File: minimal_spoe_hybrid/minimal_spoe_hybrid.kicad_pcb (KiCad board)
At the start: 4 copper layers, 25.4 x 20.3 mm, 4 parts, among them J1 TBP02R2-381-03BE

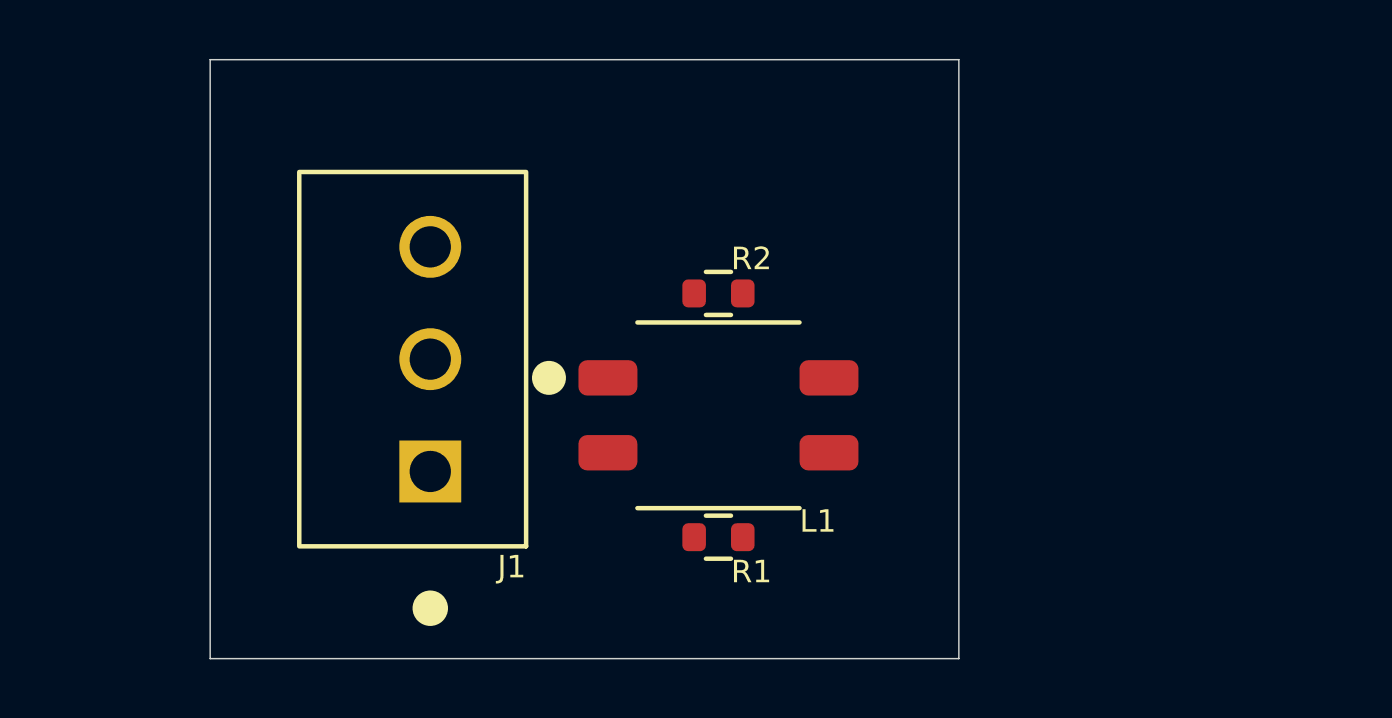
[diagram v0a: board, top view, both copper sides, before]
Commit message: Update KiCAD Symbol Generator submodule and modify project settings
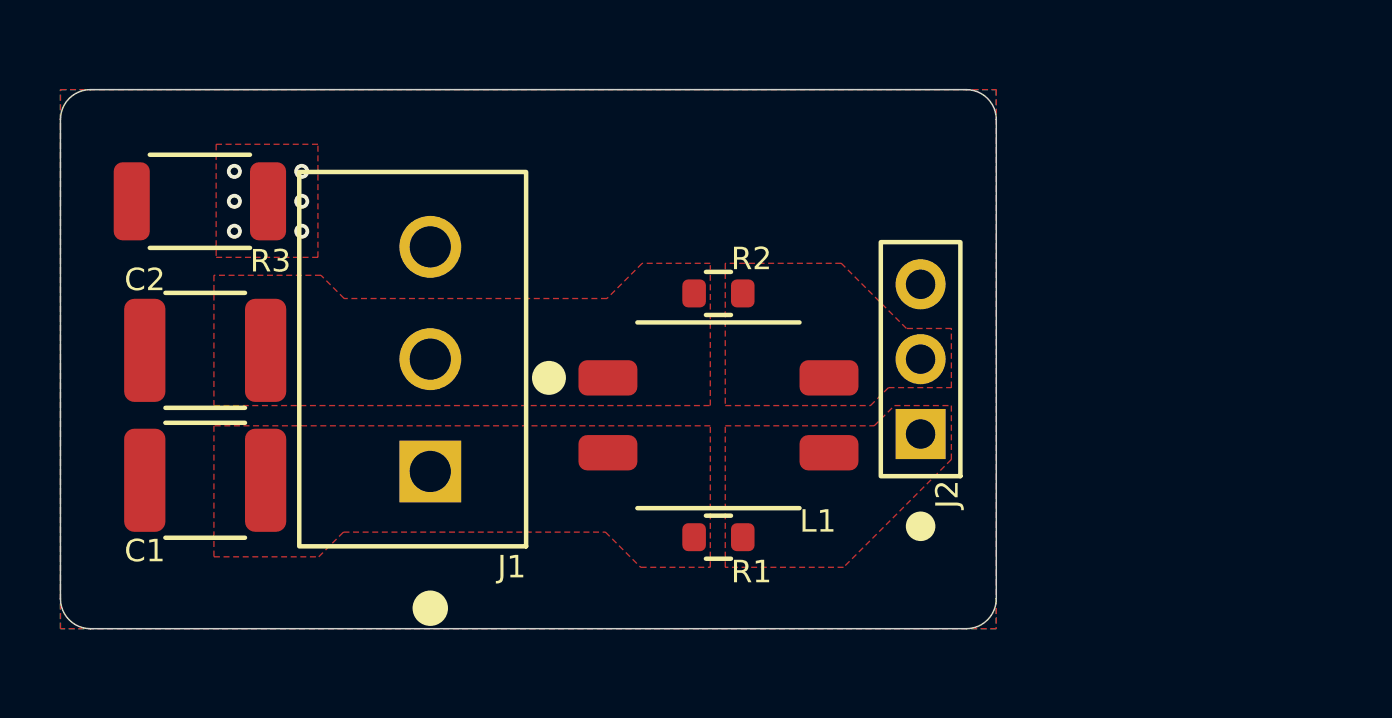
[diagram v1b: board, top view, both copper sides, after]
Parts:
- added C1: 100 pF, capacitor_footprints:C_1812_4532Metric, F.Cu at (121.5, 112.8)
- added C2: 100 pF, capacitor_footprints:C_1812_4532Metric, F.Cu at (121.5, 108.4)
- added J2: TSW-103-14-G-S, connector_footprints:TSW-103-14-G-S, F.Cu at (145.8, 108.7)
- added R3: 4.7 MΩ, resistor_footprints:R_2010_5025Metric, F.Cu at (121.3, 103.3)
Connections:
- net Net-(J1-Pad1) renamed /CABLE+
- net Net-(J1-Pad2) renamed /CABLE-
- net Net-(L1-Pad3) renamed /DATA_AND_POWER_P
- net Net-(L1-Pad4) renamed /DATA_AND_POWER_N
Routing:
- net GND: vias 0 -> 6
- added copper zone on F.Cu, net /CABLE+
- added copper zone on F.Cu, net /CABLE-
- added copper zone on F.Cu, net /DATA_AND_POWER_N
- added copper zone on F.Cu, net /DATA_AND_POWER_P
- added copper zone on F.Cu, net Earth
- added copper zone on In1.Cu, net Earth
- added copper zone on In2.Cu, net Earth
- added copper zone on B.Cu, net GND
- added copper zone on F.Cu, net GND
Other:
- board size 25.4 x 20.3 mm -> 31.8 x 18.3 mm

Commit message: Update KiCAD Symbol Generator submodule and modify project configuration
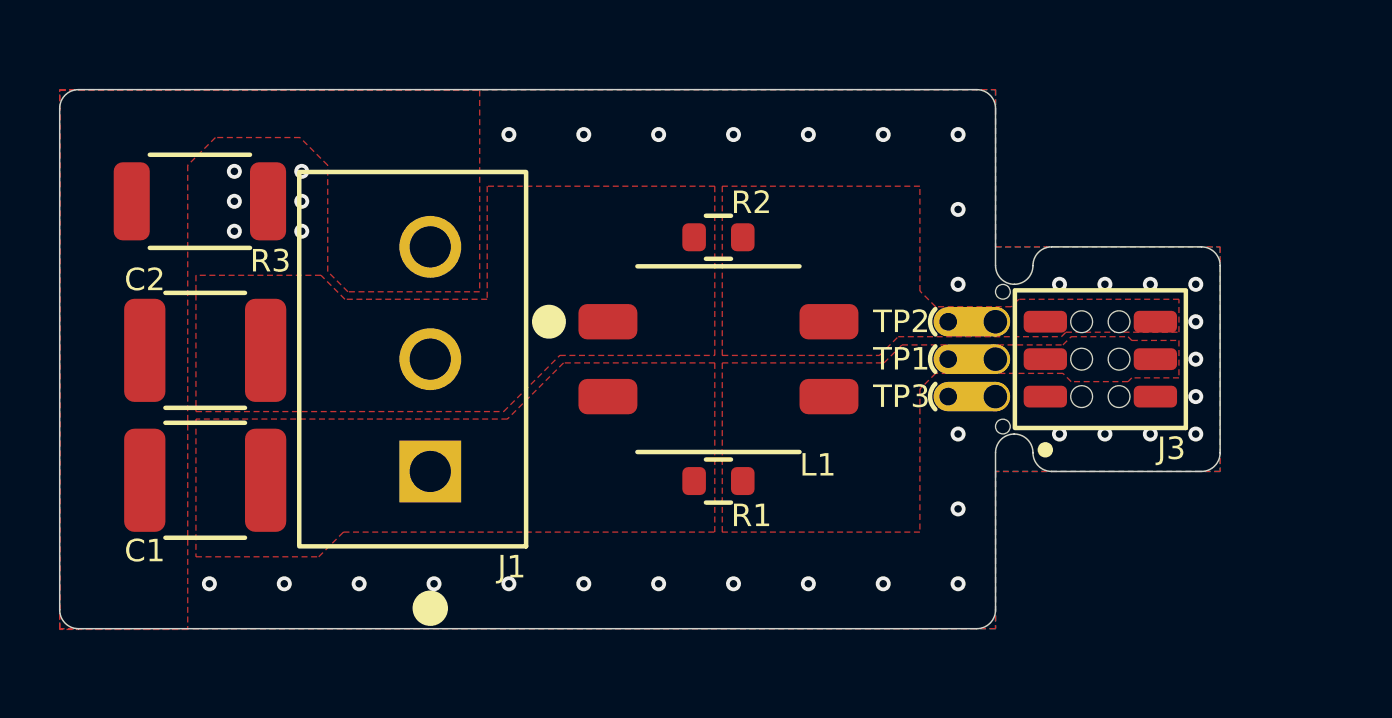
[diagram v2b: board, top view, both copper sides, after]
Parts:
- removed J2: TSW-103-14-G-S, connector_footprints:TSW-103-14-G-S
- added J3: CLP-103-02-G-D-BE, connector_footprints:CLP-103-02-G-D-BE, F.Cu at (151.9, 108.7)
- added MB1: mouse-bite-midle-50mil-200mil, mouse_bite_footprints:mouse-bite-midle-50mil-250mil, F.Cu at (149.0, 108.7)
- added TP1: TestPoint, test_point_footprints:TestPoint_THTPad_Castelated, F.Cu at (148.3, 108.7)
- added TP2: TestPoint, test_point_footprints:TestPoint_THTPad_Castelated, F.Cu at (148.3, 107.4)
- added TP3: TestPoint, test_point_footprints:TestPoint_THTPad_Castelated, F.Cu at (148.3, 110.0)
- moved L1 1.91 mm to (138.9, 108.7)
- moved R1 1.91 mm to (138.9, 112.8)
- moved R2 1.91 mm to (138.9, 104.6)
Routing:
- net GND: vias 6 -> 39
- added copper zone on In1.Cu, net GND
- added copper zone on In2.Cu, net GND
- removed copper zone on In2.Cu, net Earth
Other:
- board size 31.8 x 18.3 mm -> 39.4 x 18.3 mm

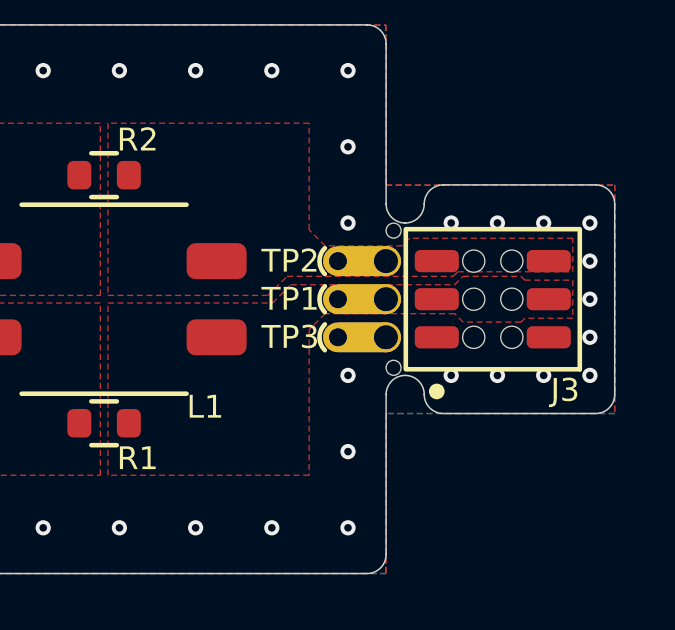
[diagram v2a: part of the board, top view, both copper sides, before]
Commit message: Update KiCAD Symbol Generator submodule and remove unused circle elements from schematic
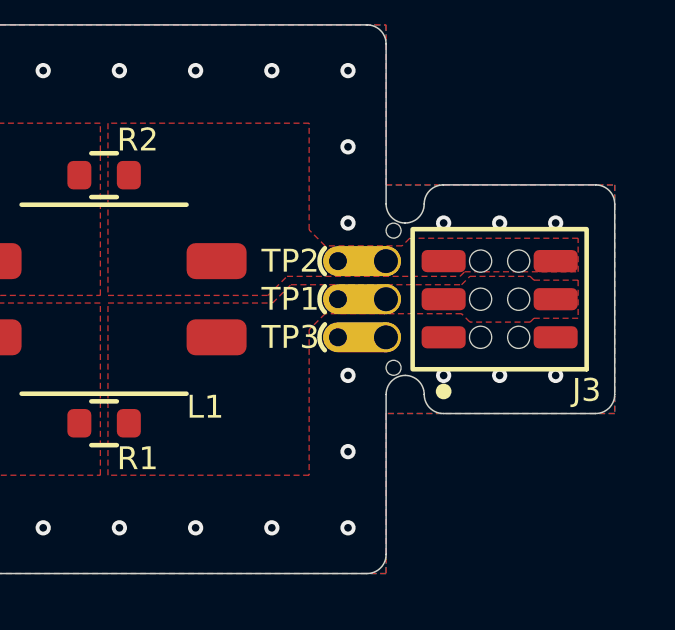
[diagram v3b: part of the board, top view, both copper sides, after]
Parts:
- moved J3 0.23 mm to (152.1, 108.7)
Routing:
- net GND: vias 39 -> 34
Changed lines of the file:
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@@
 	(footprint "connector_footprints:CLP-103-02-G-D-BE"
 		(layer "F.Cu")
-		(at 151.8921 108.6866 90)
+		(at 152.1207 108.6866 90)
 		(property "Reference" "J3"
 			(at -2.589 2.9 0)
@@
 					(thickness 0.1524)
 				)
-				(justify right top)
+				(justify top)
 			)
 		)
@@
 	)
 	(via
-		(at 155.129099 109.9566)
-		(size 0.508)
-		(drill 0.254)
-		(layers "F.Cu" "B.Cu")
-		(free yes)
-		(net 4)
-	)
-	(via
 		(at 129.286 116.3066)
 		(size 0.508)
@@
 	)
 	(via
-		(at 150.506099 106.1466)
-		(size 0.508)
-		(drill 0.254)
-		(layers "F.Cu" "B.Cu")
-		(free yes)
-		(net 4)
-	)
-	(via
-		(at 150.506099 111.2266)
+		(at 150.2537 106.1466)
+		(size 0.508)
+		(drill 0.254)
+		(layers "F.Cu" "B.Cu")
+		(free yes)
+		(net 4)
+	)
+	(via
+		(at 150.2537 111.2266)
 		(size 0.508)
 		(drill 0.254)
@@
 	)
 	(via
-		(at 152.047099 106.1466)
+		(at 152.1207 106.1466)
 		(size 0.508)
 		(drill 0.254)
@@
 	)
 	(via
-		(at 155.129099 108.6866)
-		(size 0.508)
-		(drill 0.254)
-		(layers "F.Cu" "B.Cu")
-		(free yes)
-		(net 4)
-	)
-	(via
-		(at 155.129099 106.1466)
-		(size 0.508)
-		(drill 0.254)
-		(layers "F.Cu" "B.Cu")
-		(free yes)
-		(net 4)
-	)
-	(via
 		(at 147.066 116.3066)
 		(size 0.508)
@@
 	)
 	(via
-		(at 152.047099 111.2266)
+		(at 152.1207 111.2266)
 		(size 0.508)
 		(drill 0.254)
@@
 	)
 	(via
-		(at 155.129099 111.2266)
-		(size 0.508)
-		(drill 0.254)
-		(layers "F.Cu" "B.Cu")
-		(free yes)
-		(net 4)
-	)
-	(via
 		(at 124.206 116.3066)
 		(size 0.508)
@@
 	)
 	(via
-		(at 153.588099 106.1466)
+		(at 153.9877 106.1466)
 		(size 0.508)
 		(drill 0.254)
@@
 	)
 	(via
-		(at 155.129099 107.4166)
-		(size 0.508)
-		(drill 0.254)
-		(layers "F.Cu" "B.Cu")
-		(free yes)
-		(net 4)
-	)
-	(via
-		(at 153.588099 111.2266)
+		(at 153.9877 111.2266)
 		(size 0.508)
 		(drill 0.254)
@@
 		(polygon
 			(pts
-				(xy 139.065 114.554) (xy 139.065 108.8136) (xy 144.5514 108.8136) (xy 145.161 108.204) (xy 150.622 108.204)
-				(xy 150.9014 107.9246) (xy 152.8318 107.9246) (xy 152.9588 108.0516) (xy 154.559 108.0516) (xy 154.559 109.3216)
-				(xy 152.9588 109.3216) (xy 152.8318 109.4486) (xy 150.9014 109.4486) (xy 150.622 109.1692) (xy 146.304 109.1692)
+				(xy 139.065 114.554) (xy 139.065 108.8136) (xy 144.5514 108.8136) (xy 145.161 108.204) (xy 150.8506 108.204)
+				(xy 151.13 107.9246) (xy 153.1366 107.9246) (xy 153.2636 108.0516) (xy 154.7368 108.0516) (xy 154.7368 109.3216)
+				(xy 153.2636 109.3216) (xy 153.1366 109.4486) (xy 151.13 109.4486) (xy 150.8506 109.1692) (xy 146.304 109.1692)
 				(xy 145.7706 109.7026) (xy 145.7706 114.554)
 			)
@@
 			(pts
 				(xy 145.7706 102.8192) (xy 139.065 102.8192) (xy 139.065 108.5596) (xy 144.399 108.5596) (xy 145.034 107.9246)
-				(xy 150.5712 107.9246) (xy 150.7236 107.7722) (xy 154.559 107.7722) (xy 154.559 106.6546) (xy 149.1234 106.6546)
+				(xy 150.7998 107.9246) (xy 150.9522 107.7722) (xy 154.7368 107.7722) (xy 154.7368 106.6546) (xy 149.1234 106.6546)
 				(xy 148.8694 106.9086) (xy 146.304 106.9086) (xy 145.7706 106.3752)
 			)

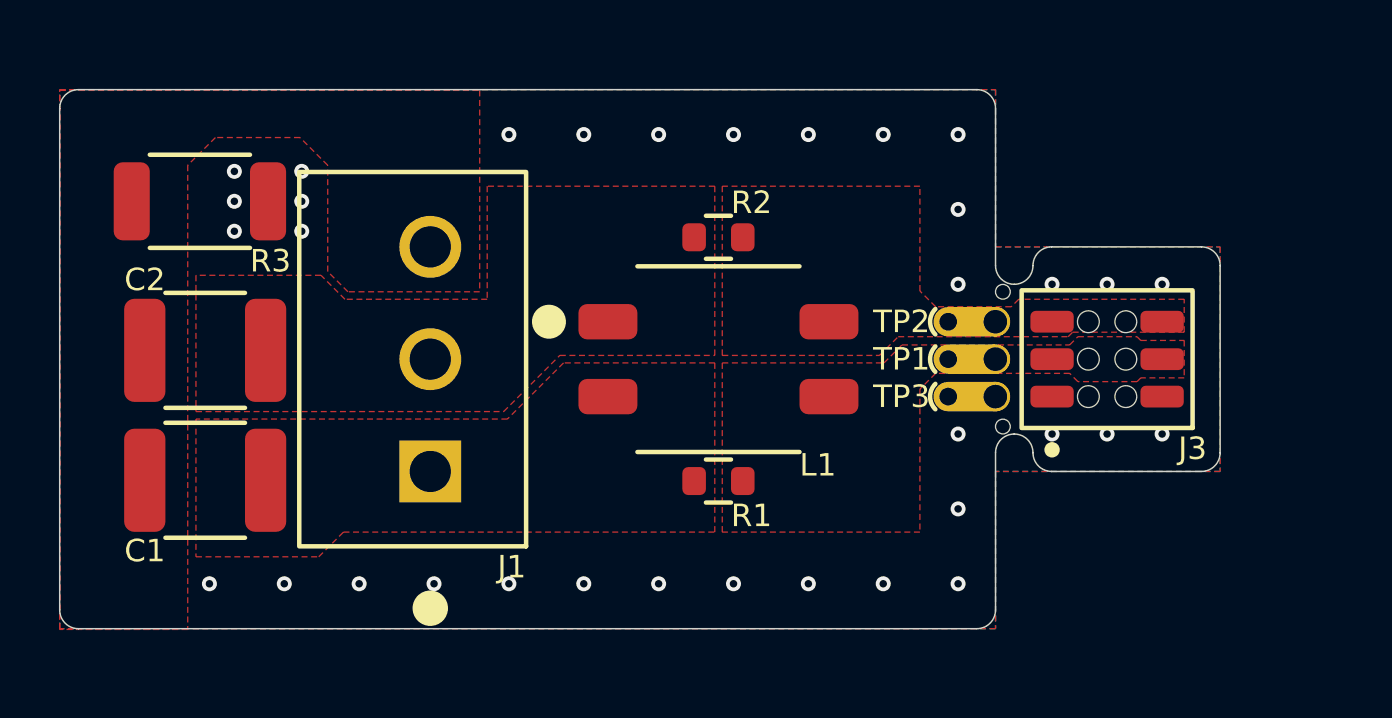
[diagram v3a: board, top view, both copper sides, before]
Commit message: Update KiCAD Symbol Generator submodule and clean up project configuration
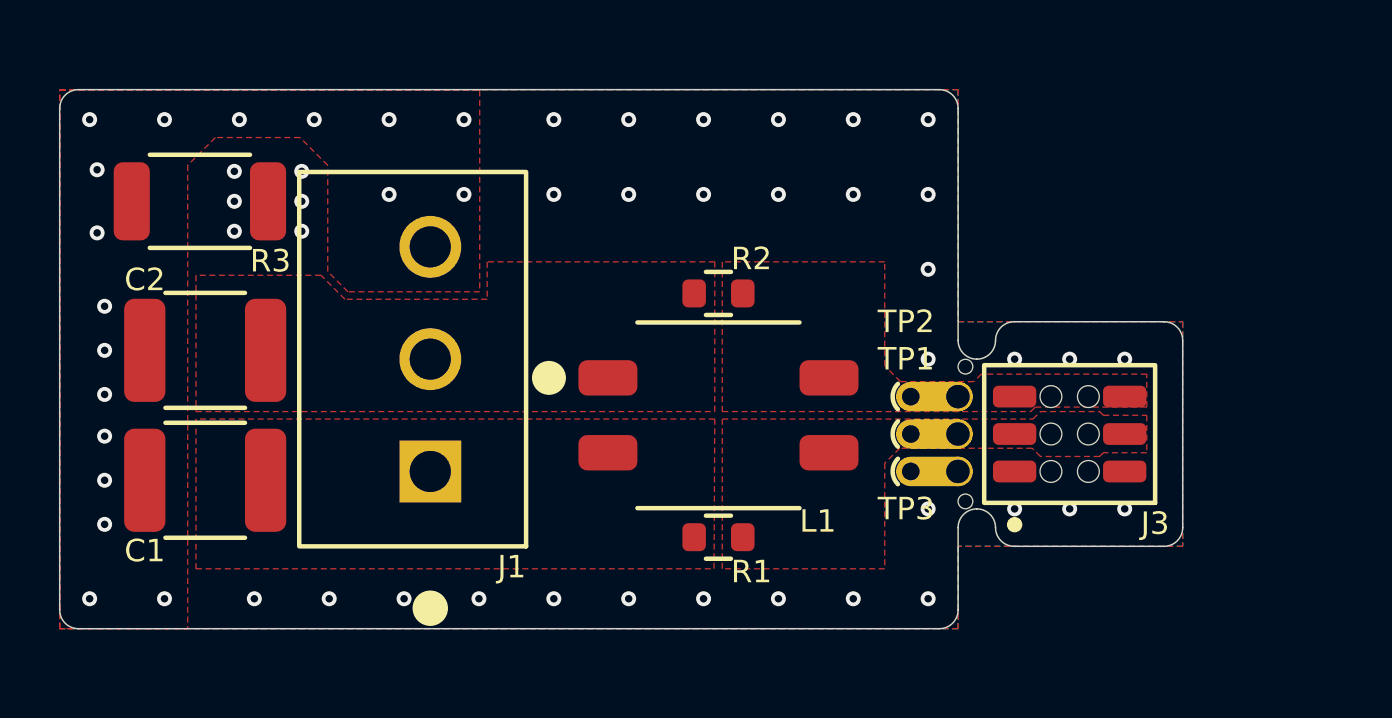
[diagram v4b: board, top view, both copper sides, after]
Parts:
- moved J3 2.84 mm to (150.9, 111.2)
- moved MB1 2.84 mm to (147.7, 111.2)
- moved TP1 2.84 mm to (147.1, 111.2)
- moved TP3 2.84 mm to (147.1, 112.5)
- moved TP2 2.84 mm to (147.1, 110.0)
- moved L1 1.91 mm to (138.9, 110.6)
- moved R1 1.91 mm to (138.9, 114.7)
- moved R2 1.91 mm to (138.9, 106.5)
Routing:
- net GND: vias 34 -> 37
- net Earth: vias 0 -> 18
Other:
- board size 39.4 x 18.3 mm -> 38.1 x 18.3 mm

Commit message: Update KiCAD Symbol Generator submodule and regenerate PDF schematic
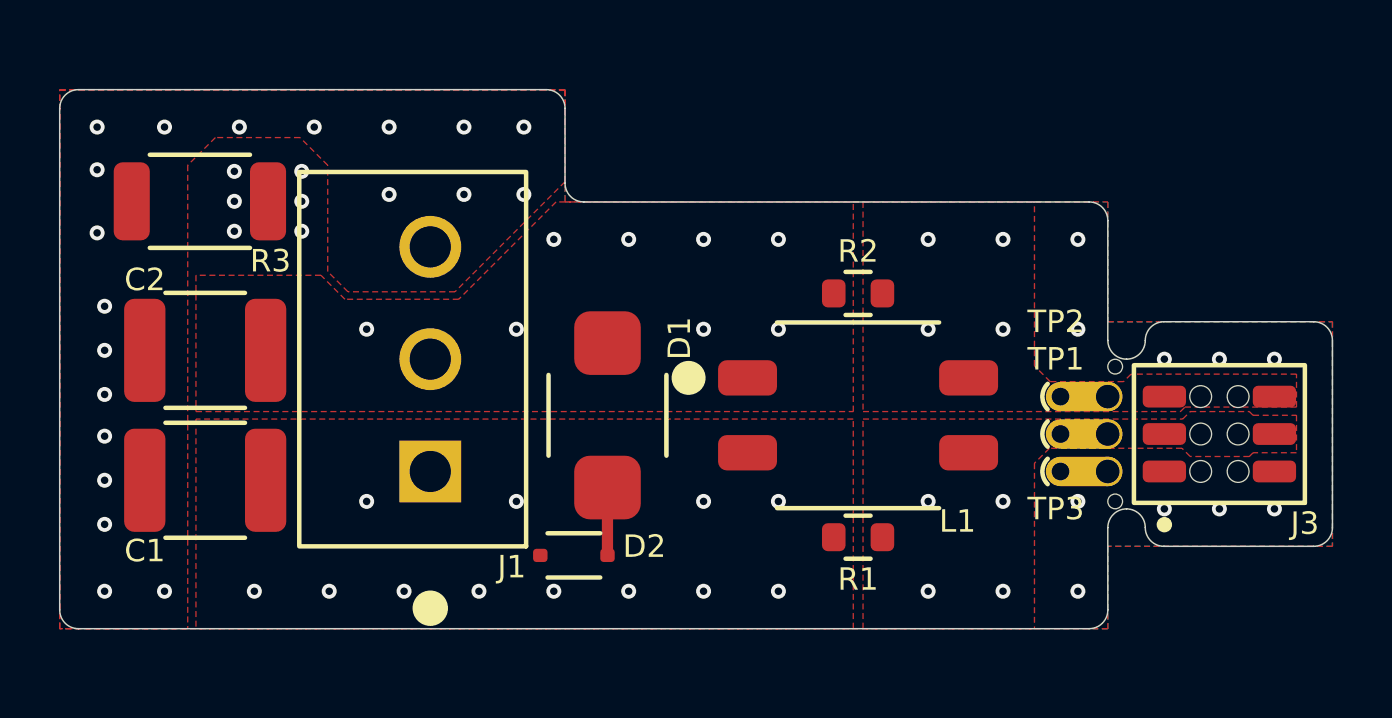
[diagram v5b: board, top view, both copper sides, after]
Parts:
- added D1: 58 V, diode_footprints:DO-214AA, F.Cu at (135.2, 110.6)
- added D2: 3.3 V, diode_footprints:SOD323, F.Cu at (134.0, 115.3)
- moved J3 5.08 mm to (155.9, 111.2)
- moved MB1 5.08 mm to (152.8, 111.2)
- moved TP1 5.08 mm to (152.1, 111.2)
- moved TP2 5.08 mm to (152.1, 110.0)
- moved TP3 5.08 mm to (152.1, 112.5)
- moved L1 4.74 mm to (143.7, 110.6)
- moved R1 4.74 mm to (143.7, 114.7)
- moved R2 4.74 mm to (143.7, 106.5)
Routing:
- net Net-(D1-Pad1): track 0.00 -> 2.30 mm
- net GND: vias 37 -> 44
- net Earth: vias 18 -> 20
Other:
- board size 38.1 x 18.3 mm -> 43.2 x 18.3 mm
